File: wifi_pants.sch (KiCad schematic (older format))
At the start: 20 parts, among them P1 CONN_02X20, U1 ESP-12E

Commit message: Add UART header, clean up routing
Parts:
- removed JP2: Jumper_NC_Small, wifi_pants:GS2, symbol Jumper_NC_Small
- added JP2: Jumper_NO_Small, wifi_pants:GS2, symbol Jumper_NO_Small
- added P2: CONN_01X06, Pin_Headers:Pin_Header_Angled_1x06, symbol CONN_01X06
- JP3: symbol Jumper_NC_Small -> Jumper_NO_Small
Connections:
- net labels added: GPIO27, PI_UART0_RXD, PI_UART0_TXD, PWM0_DAC_R, PWM1_DAC_L
- net labels removed: GPIO26
- wire segments 66 -> 69
- no-connect marks 34 -> 33
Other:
- note added: "CHIP_EN source:\nGPIO5 jumper shorted by trace\nGPIO27 alternate if SD_D3 can be\n separately remapped"
- note added: "Solder JP3 in ICT\nafter disabling\nQSPI mode on\nmodule\n"
- moved on the sheet: R1, R2, R3, R4, R5

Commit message: Add audio and expanded header
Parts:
- removed P2: CONN_01X06, Pin_Headers:Pin_Header_Angled_1x06, symbol CONN_01X06
- added C2, C3: 33nF, Capacitors_SMD:C_0805_HandSoldering, symbol C
- added C4, C5: 10uF, Capacitors_SMD:C_0805_HandSoldering, symbol C
- added JP7: Jumper_NO_Small, wifi_pants:GS2, symbol Jumper_NO_Small
- added P2: CONN_01X10, Pin_Headers:Pin_Header_Angled_1x10, symbol CONN_01X10
- added R6, R7: 270, Resistors_SMD:R_0603_HandSoldering, symbol R
- added R8, R9: 150, Resistors_SMD:R_0603_HandSoldering, symbol R
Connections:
- net labels added: +5V
- wire segments 69 -> 95
- no-connect marks 33 -> 30

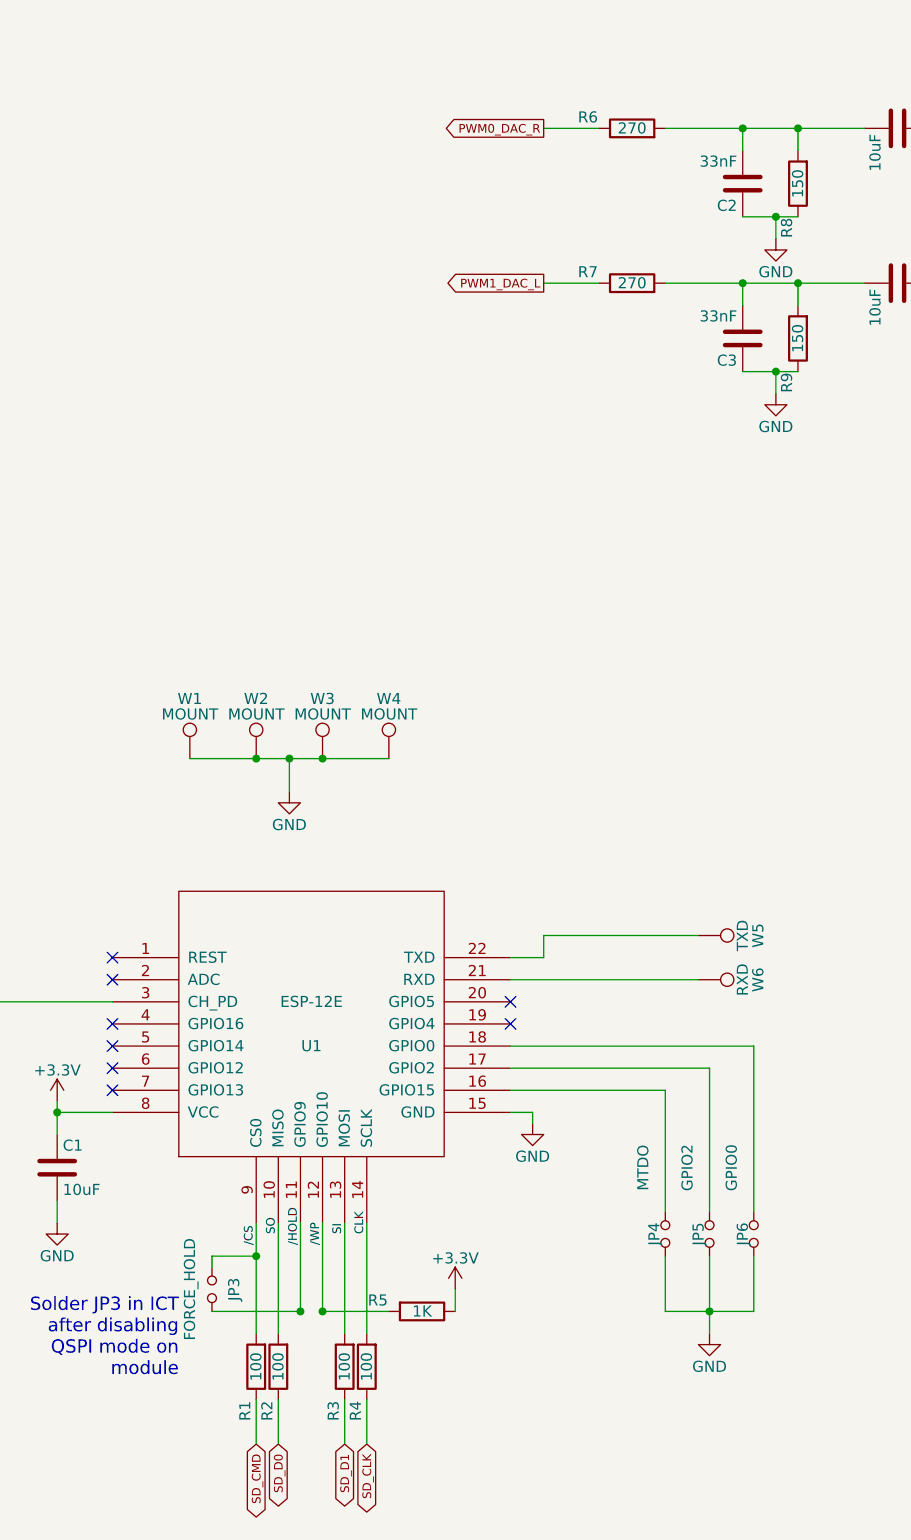
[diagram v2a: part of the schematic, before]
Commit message: Add audio, change header to include audio and +5V in, cleanup silk
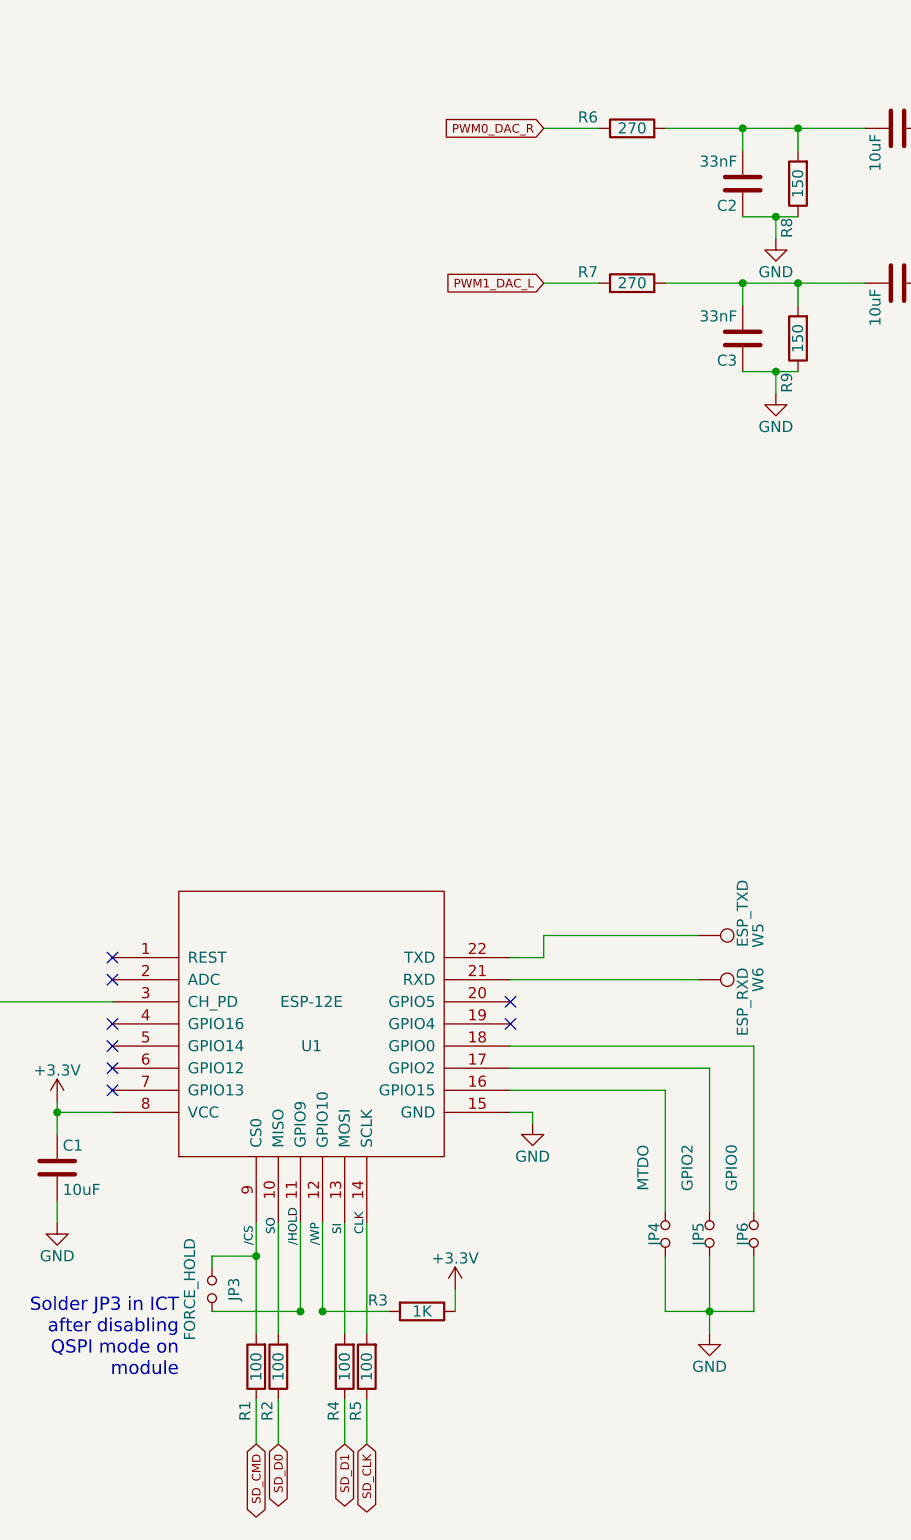
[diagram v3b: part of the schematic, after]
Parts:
- removed W1, W2, W3, W4: MOUNT, wifi_pants:NPTH_Hole_2_75mm, symbol TEST_1P
- JP1: value Jumper_NO_Small -> 27
- JP2: value Jumper_NO_Small -> 5
- JP7: value Jumper_NO_Small -> EXT_5V
- W5: value TXD -> ESP_TXD
- W6: value RXD -> ESP_RXD
- renumbered R5 to R3, R3 to R4, R4 to R5
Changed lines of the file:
@@
 Sheet 1 1
 Title "ESP8266 WiFi Module for Raspberry Pi"
-Date "2016-01-11"
+Date "2016-01-16"
 Rev "v0.1"
 Comp "Andrew Litt"
 Comment1 "https://github.com/al177/wifi_pants"
-Comment2 ""
+Comment2 "Licensed under Creative Commons Attribution Share-Alike"
 Comment3 ""
 Comment4 ""
@@
 P 5650 5050
 F 0 "W5" H 5650 5320 50  0000 C CNN
-F 1 "TXD" H 5650 5250 50  0000 C CNN
+F 1 "ESP_TXD" H 5550 5250 50  0000 C CNN
 F 2 "wifi_pants:Measurement_Point_Round-SMD-Pad_Small" H 5850 5050 50  0001 C CNN
 F 3 "" H 5850 5050 50  0000 C CNN
@@
 P 5650 5250
 F 0 "W6" H 5650 5520 50  0000 C CNN
-F 1 "RXD" H 5650 5450 50  0000 C CNN
+F 1 "ESP_RXD" H 5750 5450 50  0000 C CNN
 F 2 "wifi_pants:Measurement_Point_Round-SMD-Pad_Small" H 5850 5250 50  0001 C CNN
 F 3 "" H 5850 5250 50  0000 C CNN
@@
 NoConn ~ 8700 3650
 NoConn ~ 9200 3650
-$Comp
-L TEST_1P W1
-U 1 1 5684B584
-P 3350 4250
-F 0 "W1" H 3350 4520 50  0000 C CNN
-F 1 "MOUNT" H 3350 4450 50  0000 C CNN
-F 2 "wifi_pants:NPTH_Hole_2_75mm" H 3550 4250 50  0001 C CNN
-F 3 "" H 3550 4250 50  0000 C CNN
-	1    3350 4250
-	1    0    0    -1
-$EndComp
-$Comp
-L TEST_1P W2
-U 1 1 5684B5F3
-P 3650 4250
-F 0 "W2" H 3650 4520 50  0000 C CNN
-F 1 "MOUNT" H 3650 4450 50  0000 C CNN
-F 2 "wifi_pants:NPTH_Hole_2_75mm" H 3850 4250 50  0001 C CNN
-F 3 "" H 3850 4250 50  0000 C CNN
-	1    3650 4250
-	1    0    0    -1
-$EndComp
-$Comp
-L TEST_1P W3
-U 1 1 5684B660
-P 3950 4250
-F 0 "W3" H 3950 4520 50  0000 C CNN
-F 1 "MOUNT" H 3950 4450 50  0000 C CNN
-F 2 "wifi_pants:NPTH_Hole_2_75mm" H 4150 4250 50  0001 C CNN
-F 3 "" H 4150 4250 50  0000 C CNN
-	1    3950 4250
-	1    0    0    -1
-$EndComp
-$Comp
-L TEST_1P W4
-U 1 1 5684B6D9
-P 4250 4250
-F 0 "W4" H 4250 4520 50  0000 C CNN
-F 1 "MOUNT" H 4250 4450 50  0000 C CNN
-F 2 "wifi_pants:NPTH_Hole_2_75mm" H 4450 4250 50  0001 C CNN
-F 3 "" H 4450 4250 50  0000 C CNN
-	1    4250 4250
-	1    0    0    -1
-$EndComp
-$Comp
-L GND #PWR08
-U 1 1 5684BB74
-P 3800 4400
-F 0 "#PWR08" H 3800 4150 50  0001 C CNN
-F 1 "GND" H 3800 4250 50  0000 C CNN
-F 2 "" H 3800 4400 50  0000 C CNN
-F 3 "" H 3800 4400 50  0000 C CNN
-	1    3800 4400
-	1    0    0    -1
-$EndComp
 $Comp
 L Jumper_NO_Small JP4
@@
 $EndComp
 $Comp
-L +3.3V #PWR09
+L +3.3V #PWR08
 U 1 1 56942D2D
 P 4550 6650
-F 0 "#PWR09" H 4550 6500 50  0001 C CNN
+F 0 "#PWR08" H 4550 6500 50  0001 C CNN
 F 1 "+3.3V" H 4550 6790 50  0000 C CNN
 F 2 "" H 4550 6650 50  0000 C CNN
@@
 CLK
 $Comp
-L GND #PWR010
+L GND #PWR09
 U 1 1 56943E14
 P 4900 5900
-F 0 "#PWR010" H 4900 5650 50  0001 C CNN
+F 0 "#PWR09" H 4900 5650 50  0001 C CNN
 F 1 "GND" H 4900 5750 50  0000 C CNN
 F 2 "" H 4900 5900 50  0000 C CNN
@@
 $EndComp
 $Comp
-L +3.3V #PWR011
+L +3.3V #PWR010
 U 1 1 56944611
 P 2750 5800
-F 0 "#PWR011" H 2750 5650 50  0001 C CNN
+F 0 "#PWR010" H 2750 5650 50  0001 C CNN
 F 1 "+3.3V" H 2750 5940 50  0000 C CNN
 F 2 "" H 2750 5800 50  0000 C CNN
@@
 NoConn ~ 8700 3850
 $Comp
-L GND #PWR012
+L GND #PWR011
 U 1 1 569477AF
 P 2750 6350
-F 0 "#PWR012" H 2750 6100 50  0001 C CNN
+F 0 "#PWR011" H 2750 6100 50  0001 C CNN
 F 1 "GND" H 2750 6200 50  0000 C CNN
 F 2 "" H 2750 6350 50  0000 C CNN
@@
 $EndComp
 $Comp
-L R R3
+L R R4
 U 1 1 5694A8F6
 P 4050 7000
-F 0 "R3" V 4100 7200 50  0000 C CNN
+F 0 "R4" V 4100 7200 50  0000 C CNN
 F 1 "100" V 4050 7000 50  0000 C CNN
 F 2 "Resistors_SMD:R_0603_HandSoldering" V 3980 7000 50  0001 C CNN
@@
 $EndComp
 $Comp
-L R R4
+L R R5
 U 1 1 5694A957
 P 4150 7000
-F 0 "R4" V 4200 7200 50  0000 C CNN
+F 0 "R5" V 4200 7200 50  0000 C CNN
 F 1 "100" V 4150 7000 50  0000 C CNN
 F 2 "Resistors_SMD:R_0603_HandSoldering" V 4080 7000 50  0001 C CNN
@@
 $EndComp
 $Comp
-L R R5
+L R R3
 U 1 1 56942A8D
 P 4400 6750
-F 0 "R5" V 4350 6550 50  0000 C CNN
+F 0 "R3" V 4350 6550 50  0000 C CNN
 F 1 "1K" V 4400 6750 50  0000 C CNN
 F 2 "Resistors_SMD:R_0603_HandSoldering" V 4330 6750 50  0001 C CNN
@@
 PI_UART0_RXD
 $Comp
-L GND #PWR013
+L GND #PWR012
 U 1 1 56970598
 P 8650 2000
-F 0 "#PWR013" H 8650 1750 50  0001 C CNN
+F 0 "#PWR012" H 8650 1750 50  0001 C CNN
 F 1 "GND" H 8650 1850 50  0000 C CNN
 F 2 "" H 8650 2000 50  0000 C CNN
@@
 P 2300 5250
 F 0 "JP1" H 2300 5330 50  0000 C CNN
-F 1 "Jumper_NO_Small" H 2310 5190 50  0001 C CNN
+F 1 "27" H 2310 5190 50  0001 C CNN
 F 2 "wifi_pants:GS2" H 2300 5250 50  0001 C CNN
 F 3 "" H 2300 5250 50  0000 C CNN
@@
 P 2300 5500
 F 0 "JP2" H 2300 5580 50  0000 C CNN
-F 1 "Jumper_NO_Small" H 2310 5440 50  0001 C CNN
+F 1 "5" H 2310 5440 50  0001 C CNN
 F 2 "wifi_pants:GS2" H 2300 5500 50  0001 C CNN
 F 3 "" H 2300 5500 50  0000 C CNN
@@
 $EndComp
 $Comp
-L +5V #PWR014
+L +5V #PWR013
 U 1 1 56999E44
 P 9300 2200
-F 0 "#PWR014" H 9300 2050 50  0001 C CNN
+F 0 "#PWR013" H 9300 2050 50  0001 C CNN
 F 1 "+5V" H 9300 2340 50  0000 C CNN
 F 2 "" H 9300 2200 50  0000 C CNN
@@
 P 7950 1250
 F 0 "JP7" H 7950 1330 50  0000 C CNN
-F 1 "Jumper_NO_Small" H 7960 1190 50  0001 C CNN
+F 1 "EXT_5V" H 7960 1190 50  0001 C CNN
 F 2 "wifi_pants:GS2" H 7950 1250 50  0001 C CNN
 F 3 "" H 7950 1250 50  0000 C CNN
@@
 $EndComp
 $Comp
-L +5V #PWR015
+L +5V #PWR014
 U 1 1 5699B60D
 P 7750 1150
-F 0 "#PWR015" H 7750 1000 50  0001 C CNN
+F 0 "#PWR014" H 7750 1000 50  0001 C CNN
 F 1 "+5V" H 7750 1290 50  0000 C CNN
 F 2 "" H 7750 1150 50  0000 C CNN
@@
 $EndComp
 $Comp
-L PWR_FLAG #FLG016
+L PWR_FLAG #FLG015
 U 1 1 5699B78B
 P 9400 2450
-F 0 "#FLG016" H 9400 2545 50  0001 C CNN
+F 0 "#FLG015" H 9400 2545 50  0001 C CNN
 F 1 "PWR_FLAG" H 9400 2630 50  0000 C CNN
 F 2 "" H 9400 2450 50  0000 C CNN
@@
 Connection ~ 9750 4200
 Wire Wire Line
-	3350 4250 4250 4250
-Connection ~ 3650 4250
-Connection ~ 3950 4250
-Wire Wire Line
-	3800 4250 3800 4400
-Connection ~ 3800 4250
-Wire Wire Line
 	4800 5150 4950 5150
 Wire Wire Line
@@
 Connection ~ 6100 1400
 $Comp
-L GND #PWR017
+L GND #PWR016
 U 1 1 5699D848
 P 6000 1900
-F 0 "#PWR017" H 6000 1650 50  0001 C CNN
+F 0 "#PWR016" H 6000 1650 50  0001 C CNN
 F 1 "GND" H 6000 1750 50  0000 C CNN
 F 2 "" H 6000 1900 50  0000 C CNN
@@
 $EndComp
 $Comp
-L GND #PWR018
+L GND #PWR017
 U 1 1 5699D8AD
 P 6000 2600
-F 0 "#PWR018" H 6000 2350 50  0001 C CNN
+F 0 "#PWR017" H 6000 2350 50  0001 C CNN
 F 1 "GND" H 6000 2450 50  0000 C CNN
 F 2 "" H 6000 2600 50  0000 C CNN
@@
 Wire Wire Line
 	7050 1850 8750 1850
-Text GLabel 4950 2100 0    39   Output ~ 0
+Text GLabel 4950 2100 0    39   Input ~ 0
 PWM1_DAC_L
-Text GLabel 4950 1400 0    39   Output ~ 0
+Text GLabel 4950 1400 0    39   Input ~ 0
 PWM0_DAC_R
 Wire Wire Line
